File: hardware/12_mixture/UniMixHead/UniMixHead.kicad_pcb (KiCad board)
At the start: 2 copper layers, 64 x 45 mm, 28 parts, among them IC1 AP7375-50W5-7, J10 Conn_01x02_Male, J11 Conn_01x02_Male, J12 Conn_01x02_Male, J13 Conn_01x03_Pin, J14 Conn_01x03_Pin, J16 Conn_01x04_Male, J17 Conn_01x04_Male, J19 Conn_01x04_Male, J25 Conn_01x04_Male, J26 Conn_01x04_Male, J27 Conn_01x04_Male, J28 Conn_01x04_Male, J29 Conn_01x04_Male, J30 Conn_01x04_Male, U10 XGZP6847A, U9 XGZP6847A

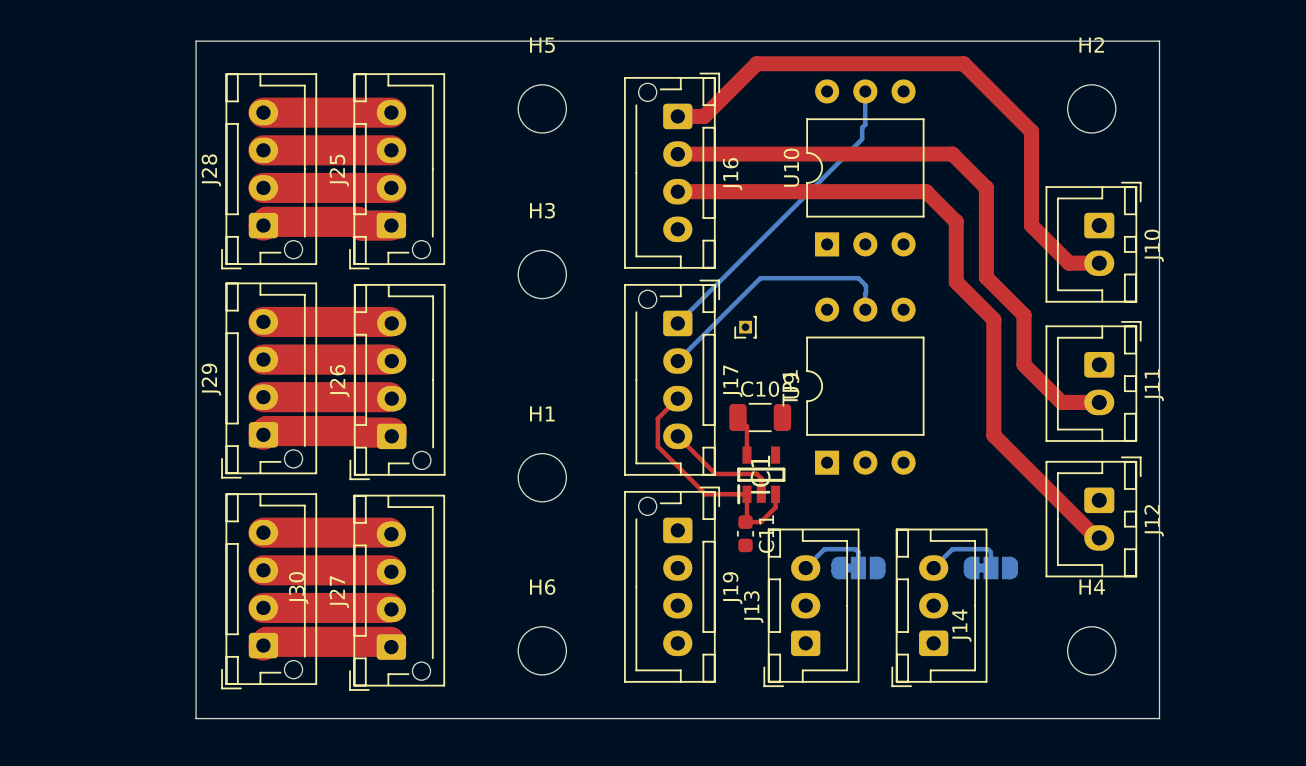
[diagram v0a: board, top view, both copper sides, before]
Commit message: Upadtes for Nucleo version
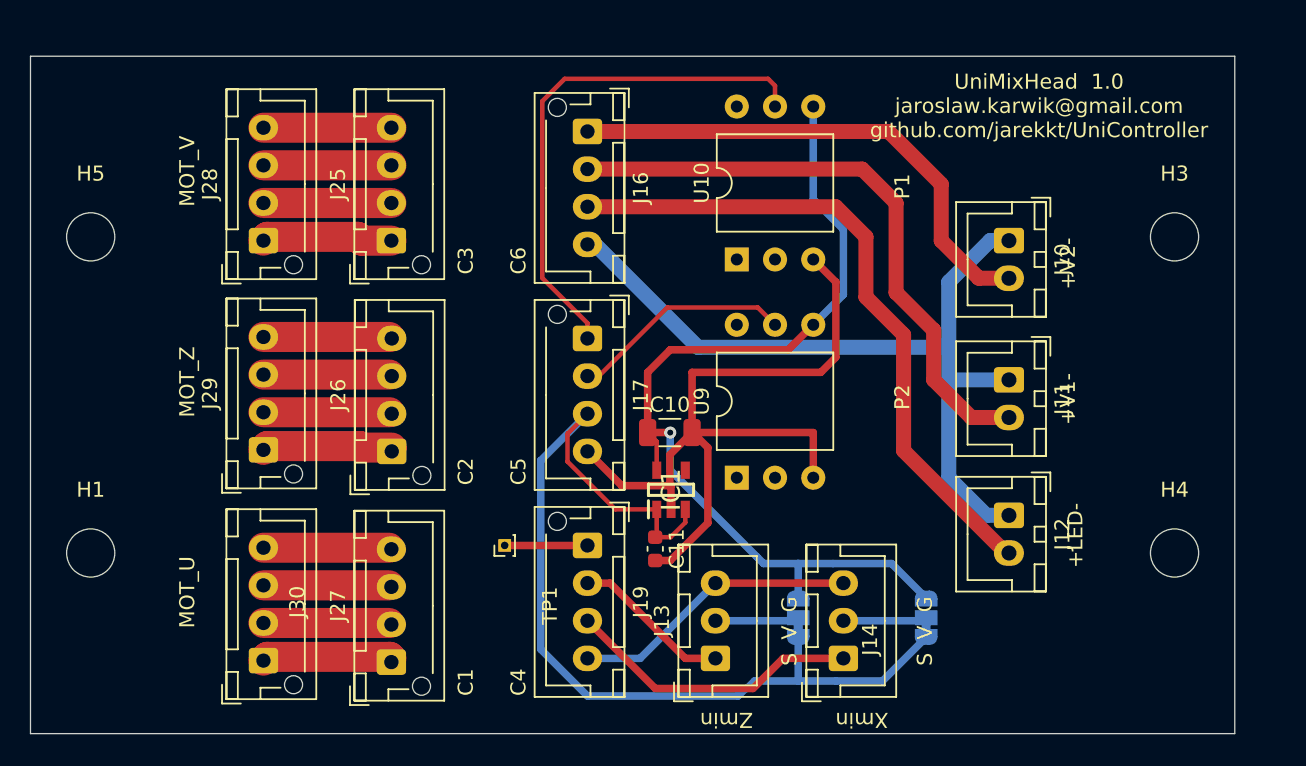
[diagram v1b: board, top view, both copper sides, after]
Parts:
- removed H2, H6: MountingHole, MountingHole:MountingHole_3.2mm_M3
- moved H3 42.1 mm to (136.0, 47.0)
- moved H5 31.2 mm to (64.0, 47.0)
- moved H1 30.4 mm to (64.0, 68.0)
- moved TP1 21.6 mm to (91.5, 67.5)
- moved H4 8.51 mm to (136.0, 68.0)
- moved C10 6.08 mm to (102.5, 60.0)
- moved C11 6.08 mm to (101.5, 67.7)
- moved IC1 6.08 mm to (102.5, 63.8)
- moved J10 6.08 mm to (125.0, 47.2)
- moved J11 6.08 mm to (125.0, 56.5)
- moved J12 6.08 mm to (125.0, 65.5)
- moved J13 6.08 mm to (105.5, 75.0)
- moved J14 6.08 mm to (114.0, 75.0)
- moved J16 6.08 mm to (97.0, 40.0)
- moved J17 6.08 mm to (97.0, 53.8)
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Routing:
- net +5VA: track 2.75 -> 62.0 mm, vias 0 -> 1
- net /MID_GND1: track 0.00 -> 54.1 mm
- net /MID_SEN_VCC: track 16.1 -> 64.5 mm
- net /MID_GND3: track 7.76 -> 55.3 mm
- net /MID_X_MIN: track 0.00 -> 19.7 mm
- net /MID_SEN1: track 20.6 -> 34.7 mm
- net /MID_Z_MIN: track 0.00 -> 10.6 mm
- net /MID_GND2: track 10.6 -> 19.1 mm
- net Net-(J14-Pin_2): track 0.00 -> 5.58 mm
- net Net-(J13-Pin_2): track 0.00 -> 5.58 mm
- net Net-(J19-Pin_1): track 0.00 -> 5.50 mm
- net /MID_VALVE1: track 38.6 -> 34.2 mm
- net /MID_SEN2: track 16.6 -> 14.8 mm
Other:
- board size 64 x 45 mm -> 80 x 45 mm
- board text added: "+LED-"
- board text added: "+V1-"
- board text added: "+V2-"
- board text added: "C1"
- board text added: "C2"
- board text added: "C3"
- board text added: "C4"
- board text added: "C5"
- board text added: "C6"
- board text added: "MOT_U"
- board text added: "MOT_V"
- board text added: "MOT_Z"
- board text added: "P1"
- board text added: "P2"
- board text added: "S V G"
- board text added: "UniMixHead 1.0 jaroslaw.karwik@gmail.com github.com/jarekkt/UniController"
- board text added: "Xmin"
- board text added: "Zmin"
